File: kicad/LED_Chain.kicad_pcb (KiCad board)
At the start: 2 copper layers, 41.1 x 28.8 mm, 14 parts, among them J1 Conn_01x07_Male, J2 L1, J3 L2, Q1 IRLML2502, Q2 IRLML2502, Q3 IRLML2502, Q4 IRLML2502, U1 HCF4027B

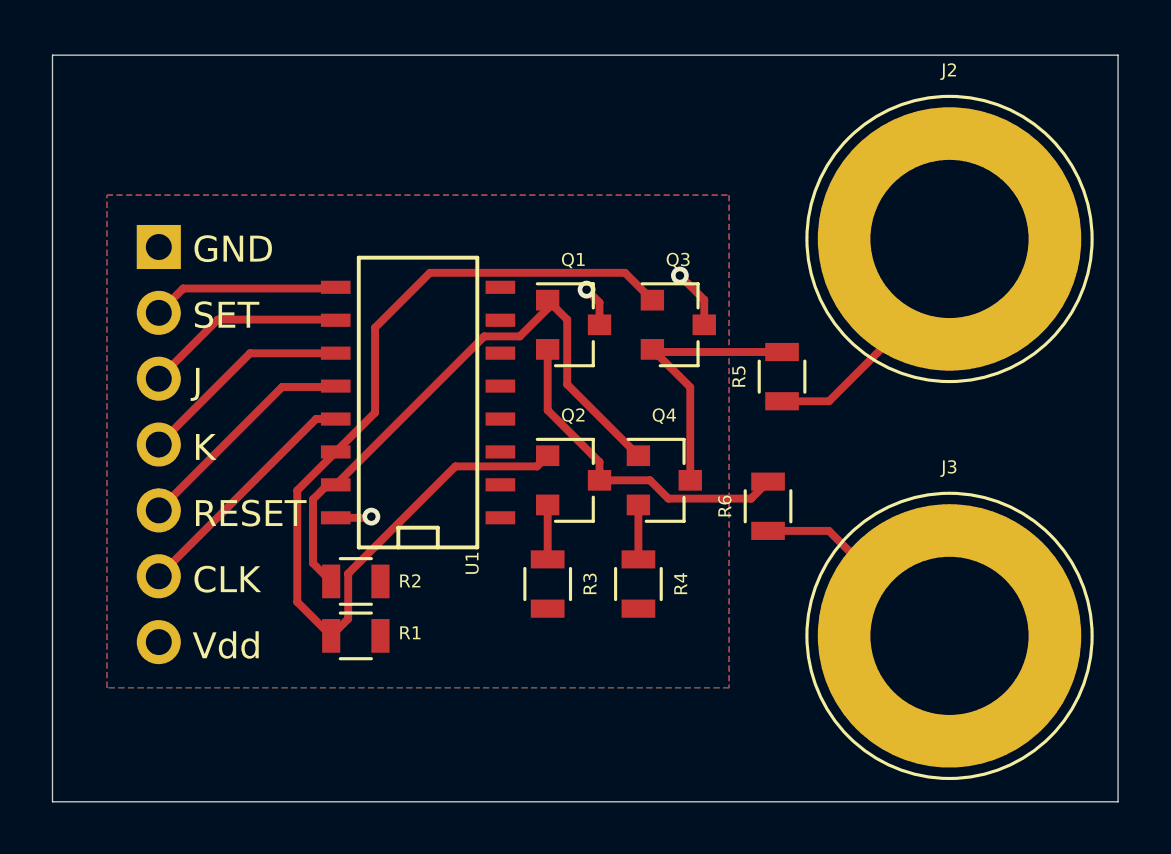
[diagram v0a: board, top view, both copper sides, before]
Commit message: Added a buffer resitor to the gates
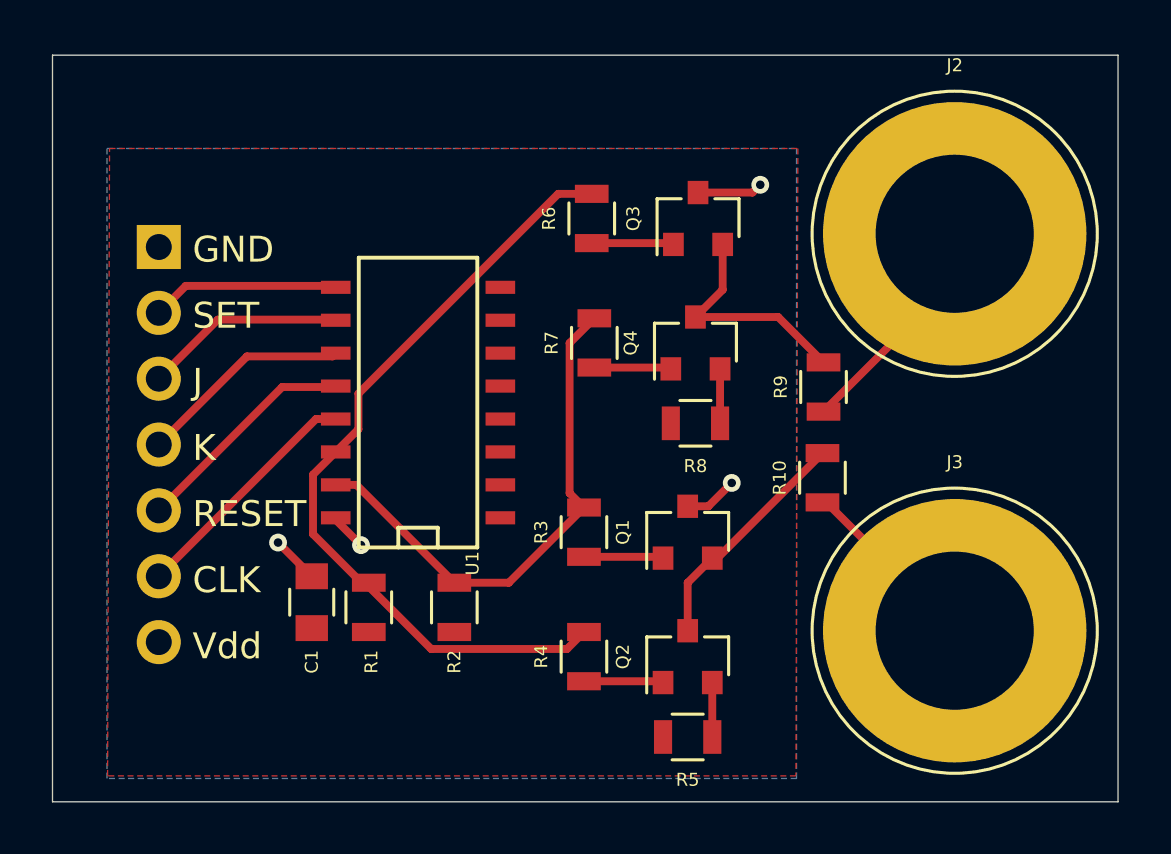
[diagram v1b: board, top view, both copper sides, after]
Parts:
- added C1: 100 nF, Capacitors_SMD:C_0805, F.Cu at (136.9, 79.7)
- added R3: 1 kΩ, Resistors_SMD:R_0805, F.Cu at (147.4, 77.0)
- added R4: 1 kΩ, Resistors_SMD:R_0805, F.Cu at (147.4, 81.8)
- added R6: 1 kΩ, Resistors_SMD:R_0805, F.Cu at (147.7, 64.9)
- added R7: 1 kΩ, Resistors_SMD:R_0805, F.Cu at (147.8, 69.7)
- moved Q1 9.13 mm to (151.4, 77.0), turned to 90 degrees
- moved Q2 8.10 mm to (151.4, 81.8), turned to 90 degrees
- moved R5 8.00 mm to (151.4, 84.9), turned to 180 degrees
- moved R8 6.58 mm to (151.7, 72.8), turned to 180 degrees
- moved Q4 5.43 mm to (151.7, 69.7), turned to 90 degrees
- moved Q3 4.17 mm to (151.8, 64.9), turned to 90 degrees
- moved R2 3.93 mm to (142.4, 79.9), turned to 270 degrees
- moved R10 2.37 mm to (156.6, 74.9)
- moved R9 1.65 mm to (156.6, 71.4)
- moved R1 1.21 mm to (139.1, 79.9), turned to 270 degrees
- moved J2 0.28 mm to (161.7, 65.5)
- moved J3 0.28 mm to (161.7, 80.8)
- renumbered R6 to R10, R3 to R5, R4 to R8, R5 to R9
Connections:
- Q1 pad 1: /Q -> Net-(Q1-Pad1)
- Q2 pad 1: /~Q -> Net-(Q2-Pad1)
- Q3 pad 1: /~Q -> Net-(Q3-Pad1)
- Q4 pad 1: /Q -> Net-(Q4-Pad1)
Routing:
- net /~Q: track 37.9 -> 31.0 mm
- net /L2: track 12.9 -> 9.12 mm
- net Net-(Q3-Pad1): track 0.00 -> 3.17 mm
- net Net-(Q2-Pad1): track 0.00 -> 3.07 mm
- net Net-(Q1-Pad1): track 0.00 -> 3.07 mm
- net /Q: track 23.3 -> 20.3 mm
- net Net-(Q4-Pad1): track 0.00 -> 2.97 mm
- net /Vdd: track 5.25 -> 7.89 mm, vias 3 -> 4
- net /L1: track 10.7 -> 8.90 mm
- net Net-(J3-Pad1): track 8.68 -> 7.15 mm
- net Net-(J2-Pad1): track 10.00 -> 8.96 mm

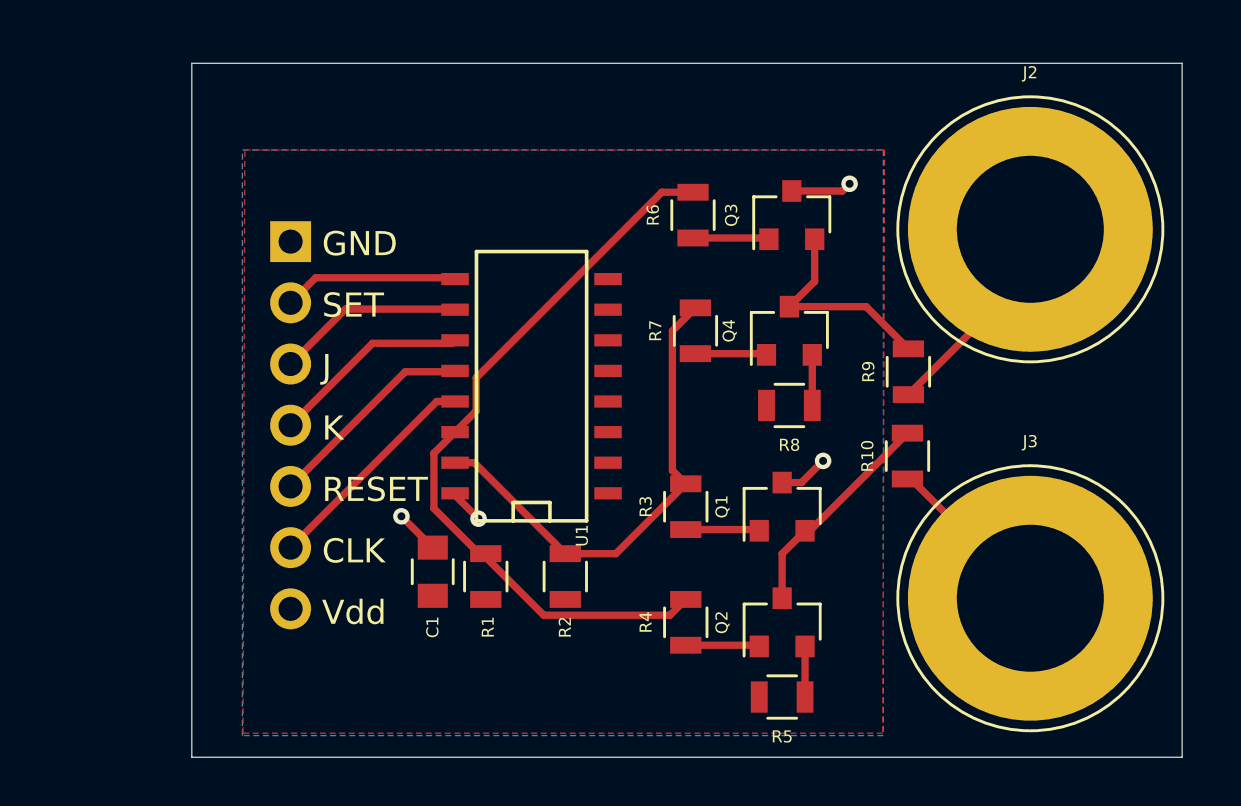
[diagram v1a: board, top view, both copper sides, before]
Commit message: Updated the schematic and started a new layout for the final design
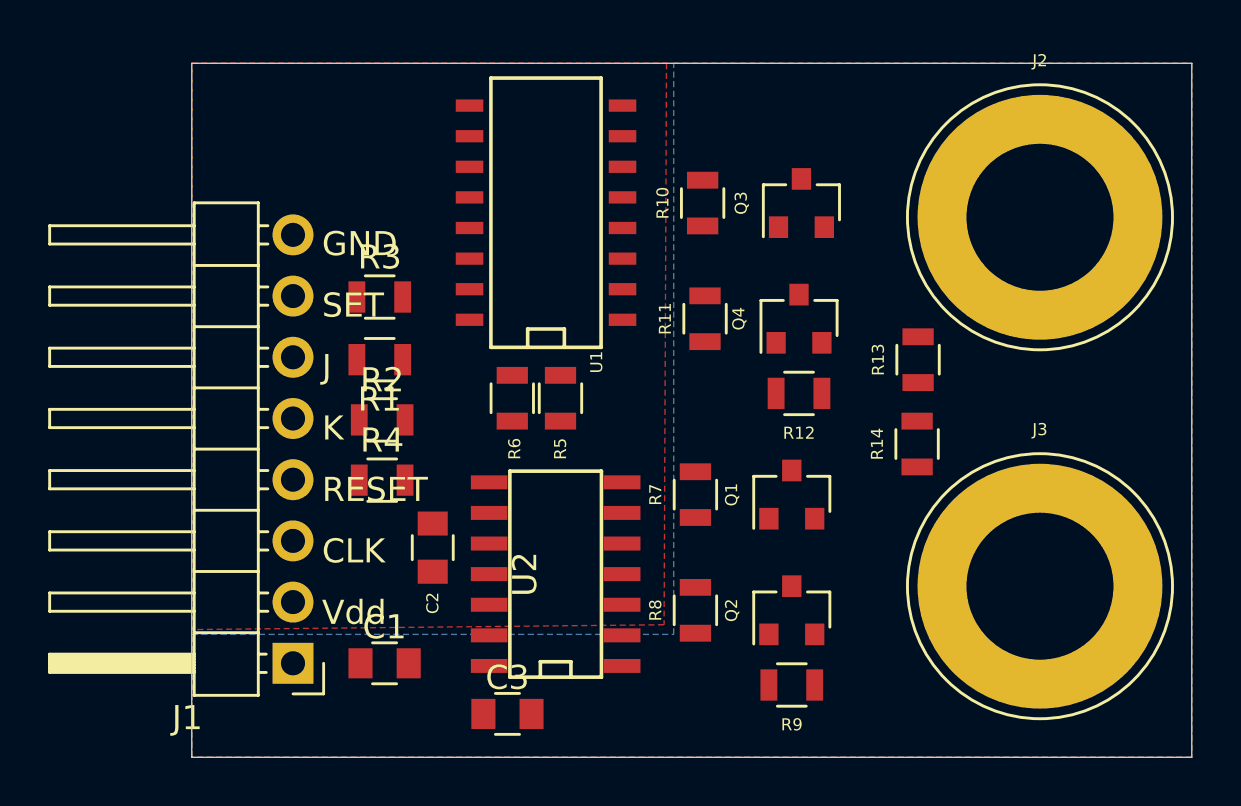
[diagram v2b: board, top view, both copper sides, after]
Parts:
- removed the R5 at (151.4, 84.9)
- removed the R6 at (147.7, 64.9)
- added C1: 1 μF, Capacitors_SMD:C_0805, F.Cu at (134.9, 83.5)
- added C3: 100 nF, Capacitors_SMD:C_0805, F.Cu at (140.0, 85.6)
- added R1: 10 kΩ, Resistors_SMD:R_0805, F.Cu at (134.7, 70.9)
- added R11: 1 kΩ, Resistors_SMD:R_0805, F.Cu at (148.2, 69.2)
- added R12: 27 Ω, Resistors_SMD:R_0805, F.Cu at (152.1, 72.3)
- added R13: 0 Ω, Resistors_SMD:R_0805, F.Cu at (157.0, 70.9)
- added R14: 0 Ω, Resistors_SMD:R_0805, F.Cu at (157.0, 74.4)
- added R2: 10 kΩ, Resistors_SMD:R_0805, F.Cu at (134.8, 73.4)
- added U2: 74LS04, LED_Chain:SOIC-14, F.Cu at (142.0, 79.8)
- J1: value Conn_01x07_Male -> Conn_01x08_Male; footprint Pin_Headers:Pin_Header_Angled_1x07_Pitch2.54mm -> Pin_Headers:Pin_Header_Angled_1x08_Pitch2.54mm; moved to F.Cu
- R10: value 0 Ω -> 1 kΩ
- R3, R4: value 1 kΩ -> 10 kΩ
- R8: value 27 Ω -> 1 kΩ
- R9: value 0 Ω -> 27 Ω
- moved J1 17.5 mm to (131.1, 83.5)
- moved R3 15.4 mm to (134.7, 68.3), turned to 0 degrees
- moved R4 13.9 mm to (134.8, 75.9), turned to 0 degrees
- moved R9 13.9 mm to (151.8, 84.4), turned to 180 degrees
- moved R10 13.5 mm to (148.1, 64.4)
- moved R8 9.35 mm to (147.8, 81.3), turned to 90 degrees
- moved R6 7.48 mm to (140.2, 72.5)
- moved R5 7.40 mm to (142.2, 72.5)
- moved U1 7.22 mm to (141.6, 64.8)
- moved R7 6.80 mm to (147.8, 76.5)
- moved C2 1.00 mm to (136.9, 78.7)
- moved J2 0.64 mm to (162.1, 65.0)
- moved J3 0.64 mm to (162.1, 80.3)
- moved Q1 0.64 mm to (151.8, 76.5)
- moved Q2 0.64 mm to (151.8, 81.3)
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- renumbered C1 to C2, R2 to R5, R1 to R6
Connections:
- C2 pad 1: /Vdd -> /Vbb
- J1 pad 1: GND -> /Vdd
- J1 pad 2: /SET -> /Vbb
- J1 pad 3: /J -> /CLK
- J1 pad 4: /K -> /RESET
- J1 pad 5: /RESET -> /K
- J1 pad 6: /CLK -> /J
- J1 pad 7: /Vdd -> /SET
- R10 pad 1: Net-(J3-Pad1) -> Net-(Q3-Pad1)
- R10 pad 2: /L2 -> /~Q
- R3 pad 1: Net-(Q1-Pad1) -> /SET
- R3 pad 2: /Q -> GND
- R4 pad 1: Net-(Q2-Pad1) -> /RESET
- R4 pad 2: /~Q -> GND
- R5 pad 1: /Q -> Net-(R5-Pad1)
- R5 pad 2: GND -> /Vbb
- R6 pad 1: /~Q -> Net-(R6-Pad1)
- R6 pad 2: GND -> /Vbb
- R7 pad 1: Net-(Q4-Pad1) -> Net-(Q1-Pad1)
- R8 pad 1: Net-(Q4-Pad2) -> Net-(Q2-Pad1)
- R8 pad 2: GND -> /~Q
- R9 pad 1: Net-(J2-Pad1) -> Net-(Q2-Pad2)
- R9 pad 2: /L1 -> GND
- U1 pad 14: /~Q -> Net-(R5-Pad1)
- U1 pad 15: /Q -> Net-(R6-Pad1)
- U1 pad 16: /Vdd -> /Vbb
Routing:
- net /~Q: track 31.0 -> 0.00 mm
- net /Q: track 20.3 -> 0.00 mm
- net /CLK: track 9.34 -> 0.00 mm
- net /L2: track 9.12 -> 0.00 mm
- net Net-(J2-Pad1): track 8.96 -> 0.00 mm
- net /L1: track 8.90 -> 0.00 mm
- net /RESET: track 8.81 -> 0.00 mm
- net /K: track 8.29 -> 0.00 mm
- net /Vdd: track 7.89 -> 0.00 mm, vias 4 -> 0
- net /J: track 7.78 -> 0.00 mm
- net /SET: track 7.28 -> 0.00 mm
- net Net-(J3-Pad1): track 7.15 -> 0.00 mm
- net Net-(Q3-Pad1): track 3.17 -> 0.00 mm
- net Net-(Q2-Pad1): track 3.07 -> 0.00 mm
- net Net-(Q1-Pad1): track 3.07 -> 0.00 mm
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- added copper zone on F.Cu, net /Vbb
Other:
- board size 41.1 x 28.8 mm -> 41.5 x 28.8 mm

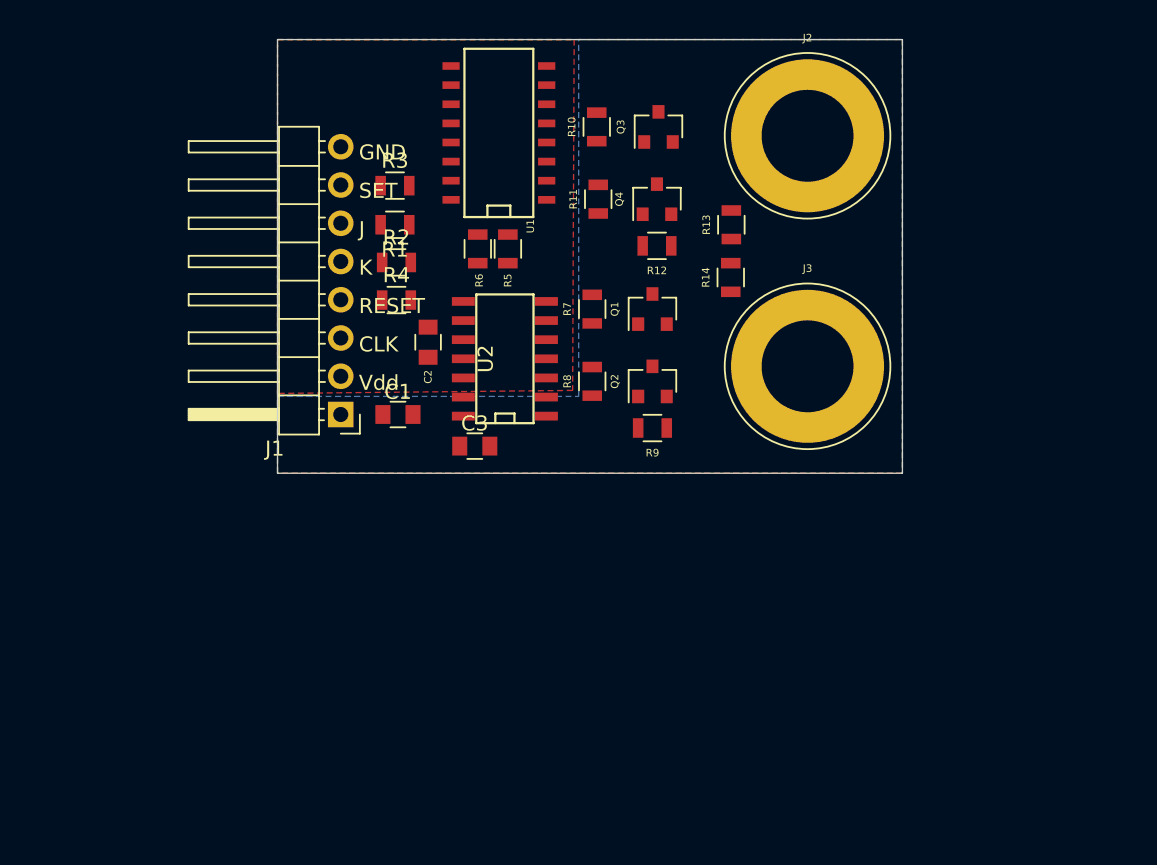
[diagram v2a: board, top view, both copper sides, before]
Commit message: Another layout attempt - changes to pin layout for Neopixel interface
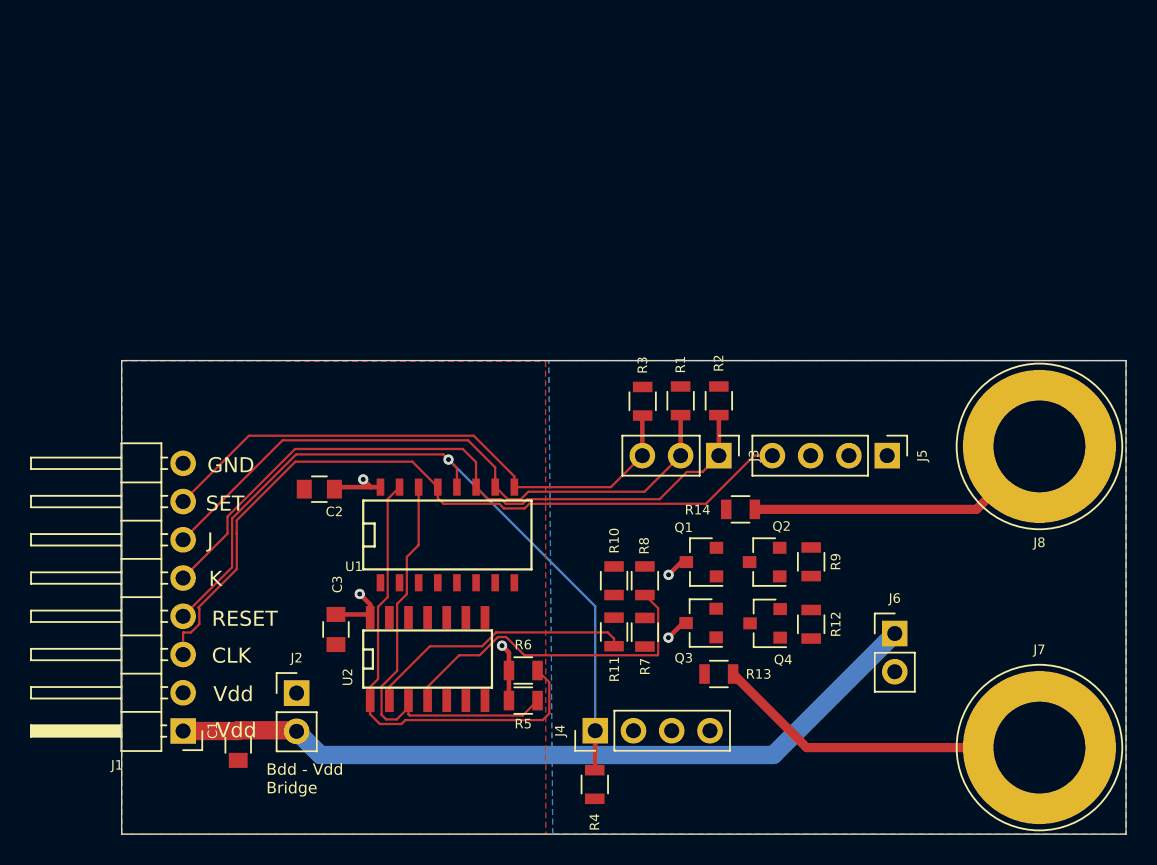
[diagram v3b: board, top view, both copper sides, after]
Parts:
- added J2: PWR, Pin_Headers:Pin_Header_Straight_1x02_Pitch2.54mm, F.Cu at (128.2, 102.0)
- added J3: NeoPixel R1 A, Pin_Headers:Pin_Header_Straight_1x03_Pitch2.54mm, F.Cu at (156.2, 86.2)
- added J4: NeoPixel R1 B, Pin_Headers:Pin_Header_Straight_1x04_Pitch2.54mm, F.Cu at (148.0, 104.5)
- added J5: NeoPixel R1 C, Pin_Headers:Pin_Header_Straight_1x04_Pitch2.54mm, F.Cu at (167.4, 86.2)
- added J6: NeoPixel R1 D, Pin_Headers:Pin_Header_Straight_1x02_Pitch2.54mm, F.Cu at (167.9, 98.0)
- J1: value Conn_01x08_Male -> Interface
- moved J7 43.5 mm to (177.5, 105.6)
- moved R4 34.8 mm to (148.0, 108.1), turned to 270 degrees
- moved Q3 33.1 mm to (155.0, 97.3), turned to 180 degrees
- moved R10 30.2 mm to (149.3, 94.5), turned to 270 degrees
- moved R5 30.0 mm to (143.2, 102.5), turned to 180 degrees
- moved R13 29.8 mm to (156.2, 100.7), turned to 180 degrees
- moved Q4 29.1 mm to (159.3, 97.4), turned to 180 degrees
- moved R11 28.8 mm to (149.3, 97.9), turned to 270 degrees
- moved R6 28.2 mm to (143.2, 100.5), turned to 180 degrees
- moved R12 27.1 mm to (162.3, 97.4), turned to 270 degrees
- moved U1 26.9 mm to (138.2, 91.5), turned to 0 degrees
- moved C1 24.4 mm to (124.3, 105.5), turned to 270 degrees
- moved J1 23.5 mm to (120.6, 104.5)
- moved R2 23.3 mm to (156.2, 82.6), turned to 90 degrees
- moved R1 22.3 mm to (153.7, 82.6), turned to 90 degrees
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- renumbered J2 to J7, J3 to J8
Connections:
- net /CLK renamed /B0
- net /J renamed /A2
- net /K renamed /A3
- net /RESET renamed /A4
- net /SET renamed /A1
- net /Vdd renamed /5V
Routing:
- net /5V: track 0.00 -> 54.4 mm, vias 0 -> 2
- net /B0: track 0.00 -> 51.1 mm
- net /A4: track 0.00 -> 50.9 mm, vias 0 -> 1
- net /A3: track 0.00 -> 46.3 mm
- net /A2: track 0.00 -> 42.1 mm
- net /A1: track 0.00 -> 37.7 mm
- net Net-(R6-Pad1): track 0.00 -> 31.5 mm
- net Net-(R5-Pad1): track 0.00 -> 28.8 mm
- net /~Q: track 0.00 -> 22.4 mm
- net Net-(J7-Pad1): track 0.00 -> 22.4 mm
- net Net-(J8-Pad1): track 0.00 -> 20.6 mm
- net /Q: track 0.00 -> 18.0 mm
- net /Vbb: track 0.00 -> 11.9 mm, vias 0 -> 3
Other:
- board size 41.5 x 28.8 mm -> 66.7 x 31.5 mm
- board text added: "Bdd - Vdd Bridge"

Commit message: Completed the layout
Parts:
- added G***: LOGO, LED_Chain:MyBasic_rounded_50_1, F.Cu at (120.2, 82.4)
- moved R5 4.68 mm to (144.9, 98.1), turned to 270 degrees
- moved R7 3.40 mm to (151.8, 94.6)
- moved R11 2.50 mm to (151.8, 98.0), turned to 90 degrees
- moved R10 2.46 mm to (149.5, 97.0), turned to 90 degrees
- moved C1 2.33 mm to (124.5, 107.8)
- moved R13 2.32 mm to (158.5, 101.0), turned to 90 degrees
- moved R14 2.24 mm to (159.8, 89.2)
- moved R8 1.98 mm to (149.6, 93.6)
- moved C2 1.72 mm to (130.2, 90.1)
- moved R6 0.64 mm to (142.7, 100.2), turned to 270 degrees
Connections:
- J5 pad 1: (no net) -> /B0
- J5 pad 4: /B0 -> (no net)
- U2 pad 1: Net-(R6-Pad1) -> (no net)
- U2 pad 10: (no net) -> /~Q
- U2 pad 11: (no net) -> Net-(R5-Pad1)
- U2 pad 12: (no net) -> /Q
- U2 pad 13: (no net) -> Net-(R6-Pad1)
- U2 pad 2: /Q -> (no net)
- U2 pad 3: Net-(R5-Pad1) -> (no net)
- U2 pad 4: /~Q -> (no net)
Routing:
- net Net-(R6-Pad1): track 31.5 -> 18.7 mm
- net Net-(Q2-Pad1): track 0.00 -> 12.2 mm
- net Net-(Q4-Pad1): track 0.00 -> 11.7 mm
- net Net-(R5-Pad1): track 28.8 -> 18.2 mm
- net /~Q: track 22.4 -> 14.1 mm
- net /L2: track 0.00 -> 6.96 mm
- net Net-(Q3-Pad1): track 0.00 -> 6.65 mm
- net /B0: track 51.1 -> 56.7 mm
- net /L1: track 0.00 -> 5.39 mm
- net GND: track 0.00 -> 5.19 mm, vias 0 -> 2
- net Net-(Q1-Pad1): track 0.00 -> 4.64 mm
- net /Vbb: track 11.9 -> 15.1 mm
- net Net-(Q2-Pad2): track 0.00 -> 2.87 mm
- net Net-(J8-Pad1): track 20.6 -> 18.2 mm
- net /5V: track 54.4 -> 56.8 mm
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- added copper zone on B.Cu, net /Vbb
- removed copper zone on F.Cu, net /Vbb
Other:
- board text added: "*"
- board text added: "A1"
- board text added: "A2"
- board text added: "A3"
- board text added: "A4"
- board text added: "A5"
- board text added: "A6"
- board text added: "A7"
- board text added: "B0 CLK"
- board text added: "B1"
- board text added: "B2"
- board text added: "B3"
- board text added: "CLK B0"
- board text added: "FF_J"
- board text added: "FF_K"
- board text added: "FF_RESET"
- board text added: "FF_SET"
- board text added: "LED Chain Driver Rev 2L_1"
- board text added: "Vbb"
- board text added: "Vdd 5V"
